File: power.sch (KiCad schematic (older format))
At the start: 48 parts, among them U1 LFE5U-85F-6BG381C, U3 TLV62569DBV, U4 TLV62569DBV, U5 TLV62569DBV

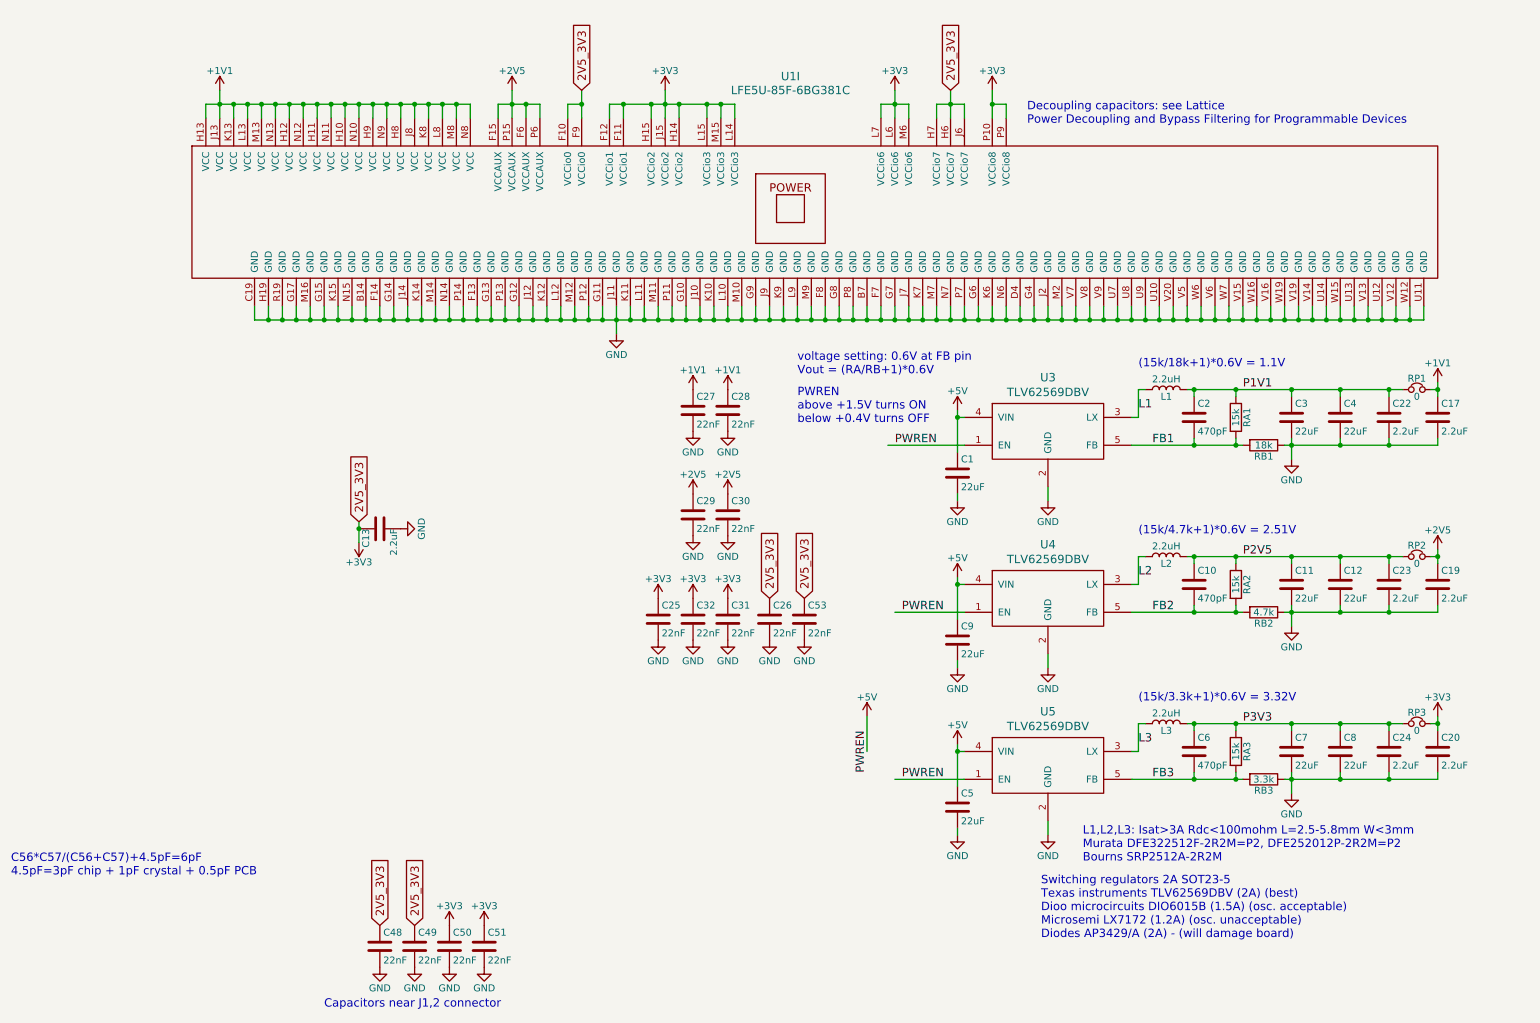
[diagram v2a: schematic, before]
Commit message: Adding DIB_V2 connector for SERDES, change battery, initial power fixes power
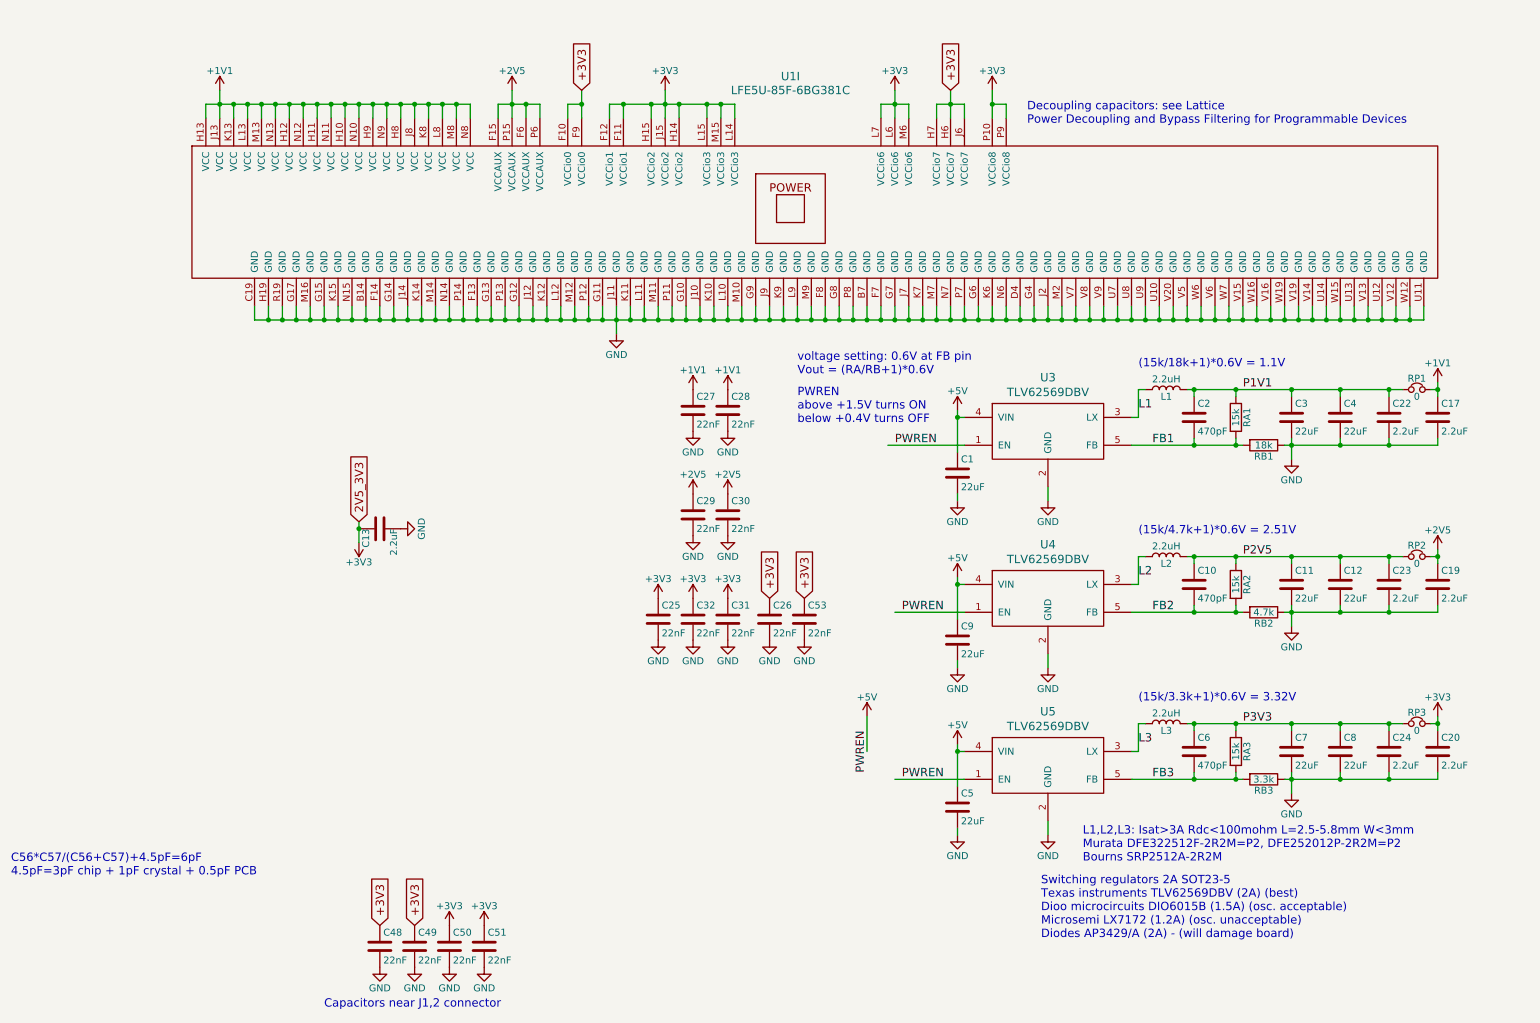
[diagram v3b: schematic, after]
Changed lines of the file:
@@
 EESchema Schematic File Version 4
-EELAYER 30 0
+LIBS:ulx3s-cache
+EELAYER 29 0
 EELAYER END
 $Descr A4 11693 8268
@@
 	7650 1050 7750 1050
 Text GLabel 4700 950  1    60   Input ~ 0
-2V5_3V3
++3V3
 Text GLabel 7350 950  1    60   Input ~ 0
-2V5_3V3
++3V3
 $Comp
 L Device:C C50
@@
 $EndComp
 Text GLabel 3250 6950 1    60   Input ~ 0
-2V5_3V3
++3V3
 $Comp
 L power:GND #PWR034
@@
 $EndComp
 Text GLabel 3500 6950 1    60   Input ~ 0
-2V5_3V3
++3V3
 Text Notes 2850 7550 0    60   ~ 0
 Capacitors near J1,2 connector
@@
 $EndComp
 Text GLabel 6300 4600 1    60   Input ~ 0
-2V5_3V3
++3V3
 Text GLabel 6050 4600 1    60   Input ~ 0
-2V5_3V3
++3V3
 $Comp
 L power:+3V3 #PWR0170

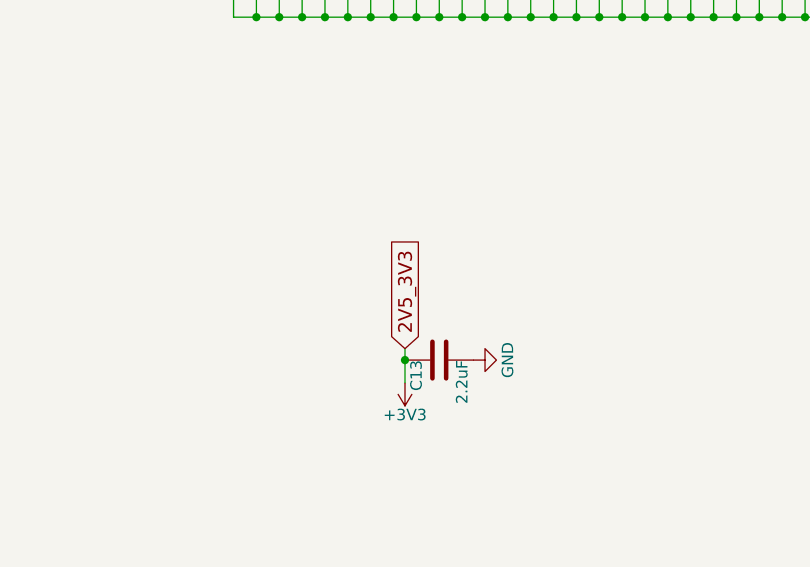
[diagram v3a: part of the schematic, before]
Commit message: Fixing 2V5_3V3 error, fixing BTN line left
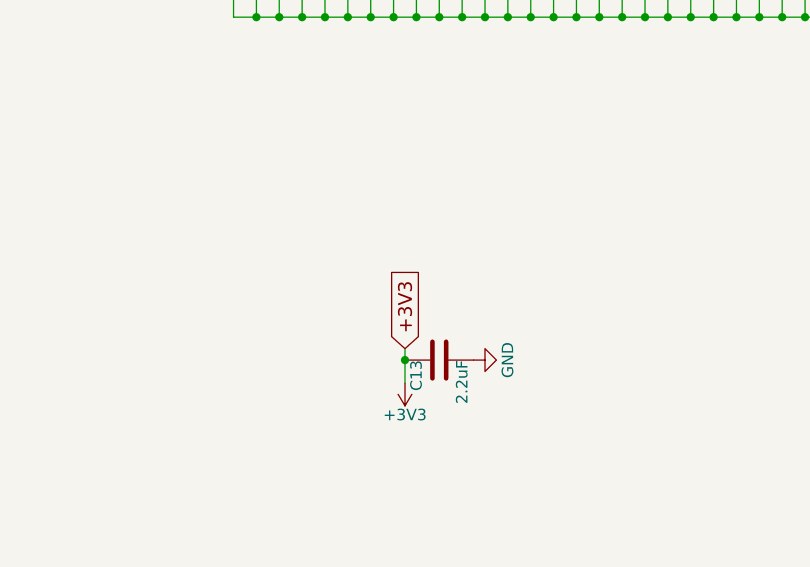
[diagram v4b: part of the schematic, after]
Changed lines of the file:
@@
 $EndComp
 Text GLabel 3100 4050 1    60   Input ~ 0
-2V5_3V3
++3V3
 Text Notes 600  6600 0    60   ~ 0
 C56*C57/(C56+C57)+4.5pF=6pF\n4.5pF=3pF chip + 1pF crystal + 0.5pF PCB
